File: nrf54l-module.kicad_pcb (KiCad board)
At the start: 4 copper layers, 16 x 25 mm, 137 parts, among them SW1 TS24CA, U1 NRF54L15-QFAA-R, U2 XL-0201SURC, U4 XL-0201SURC, U5 XL-0201SURC, U6 TLV62569DRLR, X1 XL7EL89CKI-111YLC-32M

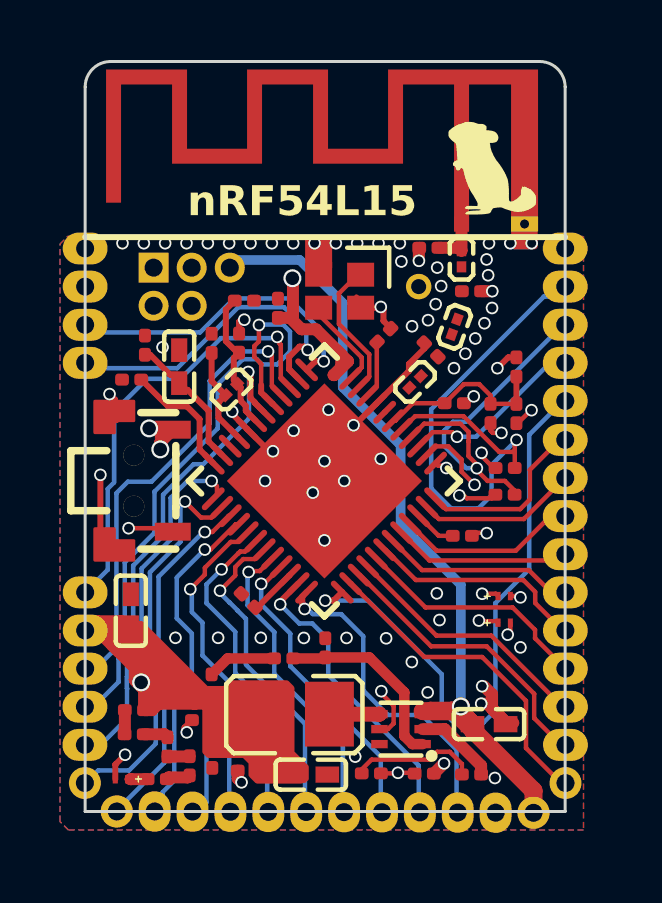
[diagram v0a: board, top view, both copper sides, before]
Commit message: feat: additinal button on P1.12
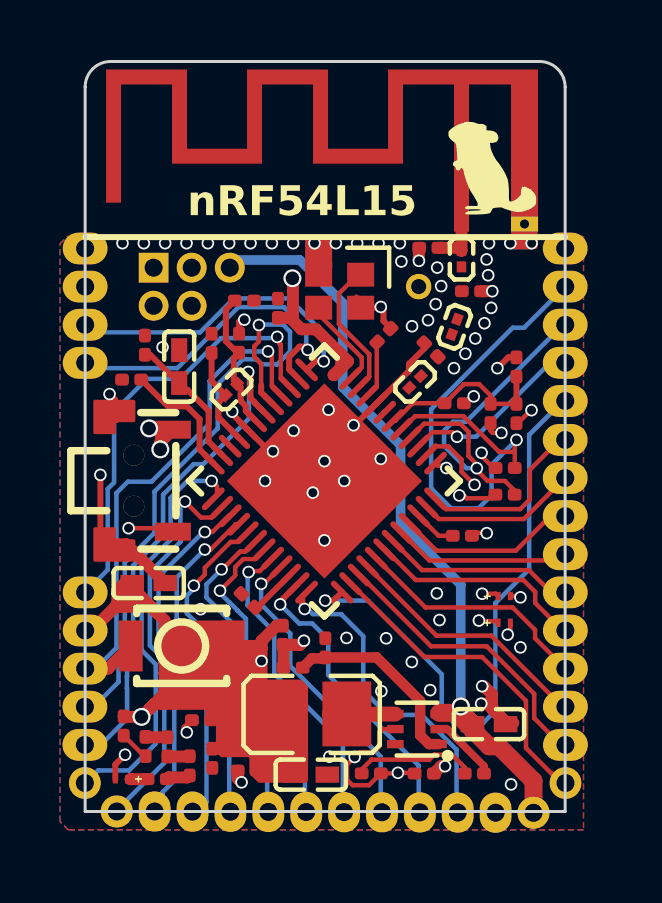
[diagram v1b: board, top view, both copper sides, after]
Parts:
- added SW2: TD-1183SN-1.7H-250, easyeda2kicad:KEY-SMD_B3U-1000PM, F.Cu at (29.0, 39.7)
- moved R3 2.87 mm to (32.4, 39.4), turned to -90 degrees
- moved C18 1.10 mm to (27.9, 37.6), turned to 0 degrees
- moved R14 0.64 mm to (27.1, 42.4), turned to 90 degrees
- moved L4 0.58 mm to (33.4, 42.0)
- moved R13 0.56 mm to (27.8, 43.1), turned to -90 degrees
- moved U6 0.53 mm to (36.9, 42.5)
- moved R4 0.44 mm to (32.7, 40.5)
- moved kibuzzard-68448BA2 0.18 mm to (27.8, 30.3)
- moved R10 0.10 mm to (38.8, 44.0)
- moved kibuzzard-684616DE 0.05 mm to (30.8, 29.4)
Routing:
- net +1V8: track 66.6 -> 90.6 mm, vias 4 -> 5
- net VIN: track 33.7 -> 29.7 mm
- net SW_EN: track 24.2 -> 26.8 mm, vias 2 -> 3
- net P1.12: track 16.4 -> 18.2 mm
- net GND: track 34.2 -> 35.9 mm, vias 70 -> 67
- net Net-(U6-SW): track 1.67 -> 2.78 mm
- net Net-(R3-Pad2): track 2.30 -> 1.53 mm, vias 0 -> 1

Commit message: chore: refactoring
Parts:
- moved U2 0.42 mm to (27.1, 43.8), turned to -90 degrees
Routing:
- net GND: track 35.9 -> 35.3 mm

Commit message: feat: 6 layer because it's cheaper lol wtf
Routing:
- added copper zone on In3.Cu, net GND
- added copper zone on In4.Cu, net GND
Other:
- copper layers 4 -> 6

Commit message: chore: refactoring
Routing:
- net GND: track 35.3 -> 39.9 mm

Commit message: chore: checkpoint
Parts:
- removed the ? at (28.1, 28.4)
- removed the ? at (36.9, 27.8)
- removed the ? at (29.4, 28.4)
- removed the ? at (29.4, 27.1)
- removed the ? at (28.1, 27.1)
- removed the ? at (30.6, 27.1)
- removed C13: 1.5pF, Capacitor_SMD:C_0201_0603Metric
- removed kibuzzard-68448B88: G***, kibuzzard-68448B88
- removed kibuzzard-68449000: G***, kibuzzard-68449000
- removed kibuzzard-6846144B: G***, kibuzzard-6846144B
- removed kibuzzard-68461451: G***, kibuzzard-68461451
- removed kibuzzard-68461457: G***, kibuzzard-68461457
- removed kibuzzard-684616DE: G***, kibuzzard-684616DE
- removed kibuzzard-6846173A: G***, kibuzzard-6846173A
- removed kibuzzard-68461772: G***, kibuzzard-68461772
- removed kibuzzard-68461788: G***, kibuzzard-68461788
- removed kibuzzard-68463A73: G***, kibuzzard-68463A73
- removed kibuzzard-68463A78: G***, kibuzzard-68463A78
- removed kibuzzard-68463A7B: G***, kibuzzard-68463A7B
- removed kibuzzard-68463A81: G***, kibuzzard-68463A81
- removed kibuzzard-68463A85: G***, kibuzzard-68463A85
- added ?: , , F.Cu at (25.8, 36.6)
- added ?: , , F.Cu at (25.8, 32.8)
- added ?: , , F.Cu at (25.8, 35.4)
- added ?: , , F.Cu at (25.8, 31.6)
- added ?: , , F.Cu at (25.8, 34.1)
- added C23: 10uF, easyeda2kicad:C0402, F.Cu at (30.1, 39.3)
- added J1: BM28B0.6-10DS/2-0.35V(51), easyeda2kicad:CONN-SMD_BM28B0.6-10DS-2-0.35V-51, F.Cu at (29.4, 27.8)
- added R15: 1kΩ, Resistor_SMD:R_0201_0603Metric, F.Cu at (39.0, 38.3)
- added R16: 1kΩ, Resistor_SMD:R_0201_0603Metric, F.Cu at (39.0, 39.7)
- added U3: XL-0201SURC, easyeda2kicad:LED-SMD_L0.65-W0.35-P0.41_XL-0201SURC, F.Cu at (38.3, 37.7)
- added U7: XL-0201SURC, easyeda2kicad:LED-SMD_L0.65-W0.35-P0.41_XL-0201SURC, F.Cu at (38.3, 39.1)
- added kibuzzard-68478C96: G***, kibuzzard-68478C96, B.Cu at (27.8, 29.1)
- added kibuzzard-68478D5A: G***, kibuzzard-68478D5A, B.Cu at (27.3, 26.5)
- added kibuzzard-68478D5E: G***, kibuzzard-68478D5E, B.Cu at (28.4, 27.8)
- added kibuzzard-68478D64: G***, kibuzzard-68478D64, B.Cu at (27.8, 31.6)
- added kibuzzard-68478D6B: G***, kibuzzard-68478D6B, B.Cu at (27.8, 32.8)
- added kibuzzard-68478D71: G***, kibuzzard-68478D71, B.Cu at (27.2, 34.1)
- added kibuzzard-68478D74: G***, kibuzzard-68478D74, B.Cu at (27.2, 35.4)
- added kibuzzard-68478D78: G***, kibuzzard-68478D78, B.Cu at (27.8, 36.6)
- added kibuzzard-68478D82: G***, kibuzzard-68478D82, B.Cu at (27.8, 38.0)
- added kibuzzard-68478D86: G***, kibuzzard-68478D86, B.Cu at (27.3, 39.2)
- added kibuzzard-68478D8D: G***, kibuzzard-68478D8D, B.Cu at (27.8, 40.5)
- added kibuzzard-68478D98: G***, kibuzzard-68478D98, B.Cu at (27.8, 41.8)
- added kibuzzard-68478D9B: G***, kibuzzard-68478D9B, B.Cu at (27.8, 43.1)
- L2, L3: value LQP03TN3N5B02D -> MLG0603P2N7CT000
- SW1: value TS24CA -> ~; footprint easyeda2kicad:SW-SMD_TS24CA -> easyeda2kicad:KEY-SMD_B3U-1000PM
- SW2: value TD-1183SN-1.7H-250 -> ~
- moved G*** 11.2 mm to (28.8, 23.1)
- moved kibuzzard-6844924F 4.73 mm to (33.9, 33.9)
- moved kibuzzard-68449253 4.73 mm to (36.3, 34.5)
- moved kibuzzard-684623CD 4.73 mm to (35.1, 34.5)
- moved kibuzzard-68449359 4.32 mm to (32.1, 38.5)
- moved kibuzzard-68449351 4.32 mm to (34.5, 38.5)
- moved kibuzzard-68449360 4.32 mm to (33.3, 38.5)
- moved C18 3.61 mm to (28.8, 41.2), turned to 180 degrees
- moved C7 2.36 mm to (39.4, 27.5), turned to 0 degrees
- moved SW2 1.94 mm to (27.9, 38.1), turned to 90 degrees
- moved C5 1.86 mm to (30.9, 30.1), turned to -90 degrees
- moved X1 1.25 mm to (35.5, 28.3)
- moved C8 1.11 mm to (37.9, 28.6), turned to 170 degrees
- moved G*** 1.10 mm to (40.4, 23.8)
- moved C11 1.03 mm to (33.3, 28.6)
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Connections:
- AE1 pad 2: (no net) -> GND
- SW1 pad 1: GND -> +1V8
- SW1 pad 2: GND -> nRESET
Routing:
- net P0.04: track 18.9 -> 38.3 mm, vias 1 -> 2
- net P0.02: track 6.39 -> 25.1 mm, vias 1 -> 2
- net P0.03: track 12.8 -> 31.3 mm, vias 1 -> 2
- net +1V8: track 90.6 -> 109.1 mm, vias 5 -> 11
- net SWDCLK: track 15.0 -> 32.8 mm, vias 1 -> 3
- net SWDIO: track 12.5 -> 26.5 mm, vias 1 -> 2
- net VIN: track 29.7 -> 39.6 mm
- net GND: track 39.9 -> 32.0 mm, vias 67 -> 80
- net P1.11: track 14.7 -> 21.3 mm, vias 1 -> 2
- net P1.09: track 10.5 -> 16.0 mm
- net P1.13: track 20.8 -> 16.5 mm
- net nRESET: track 41.1 -> 44.8 mm, vias 2 -> 3
- net SW_EN: track 26.8 -> 23.7 mm
- net P1.12: track 18.2 -> 21.2 mm, vias 1 -> 2
- net P1.10: track 10.9 -> 13.6 mm, vias 1 -> 2
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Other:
- board size 16 x 25 mm -> 16.4 x 25.2 mm
- board text added: "16"
- board text added: "2.5V ≤ VIN ≤ 5.5V"
- board text removed: "01"
- board text removed: "1.8V ≤ VIN ≤ 5.5V"

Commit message: chore: checkpoint
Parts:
- removed the C14 at (38.1, 31.6)
- removed FB1: BLM03PX121SN1D, easyeda2kicad:L0201
- removed R12, R13, R14, R15, R16: 1kΩ, Resistor_SMD:R_0201_0603Metric
- removed the R2 at (28.2, 44.2)
- removed the U2 at (27.2, 43.8)
- removed U3, U4, U5, U7: XL-0201SURC, easyeda2kicad:LED-SMD_L0.65-W0.35-P0.41_XL-0201SURC
- removed kibuzzard-68448BA2: G***, kibuzzard-68448BA2
- removed kibuzzard-68448DE0: G***, kibuzzard-68448DE0
- removed kibuzzard-68448DE9: G***, kibuzzard-68448DE9
- removed kibuzzard-68448E11: G***, kibuzzard-68448E11
- removed kibuzzard-68448E3B: G***, kibuzzard-68448E3B
- removed kibuzzard-68448E4C: G***, kibuzzard-68448E4C
- removed kibuzzard-68448E55: G***, kibuzzard-68448E55
- removed kibuzzard-684495B0: G***, kibuzzard-684495B0
- removed kibuzzard-684495B4: G***, kibuzzard-684495B4
- removed kibuzzard-684495B8: G***, kibuzzard-684495B8
- removed kibuzzard-684617E6: G***, kibuzzard-684617E6
- removed kibuzzard-684623E2: G***, kibuzzard-684623E2
- removed kibuzzard-68478C96: G***, kibuzzard-68478C96
- removed kibuzzard-68478D64: G***, kibuzzard-68478D64
- removed kibuzzard-68478D6B: G***, kibuzzard-68478D6B
- removed kibuzzard-68478D74: G***, kibuzzard-68478D74
- removed kibuzzard-68478D78: G***, kibuzzard-68478D78
- removed kibuzzard-68478D82: G***, kibuzzard-68478D82
- added C11: 2.2uF, Capacitor_SMD:C_0201_0603Metric, F.Cu at (30.3, 41.4)
- added LED1: TZ-P2-0402RTIA1-0.45T, easyeda2kicad:LED0402-RD_RED, F.Cu at (27.4, 27.6)
- added LED2: TZ-P2-0402RTIA1-0.45T, easyeda2kicad:LED0402-RD_RED, F.Cu at (28.4, 27.6)
- added LED3: TZ-P2-0402RTIA1-0.45T, easyeda2kicad:LED0402-RD_RED, F.Cu at (27.4, 29.7)
- added LED4: TZ-P2-0402RTIA1-0.45T, easyeda2kicad:LED0402-RD_RED, F.Cu at (28.4, 29.7)
- added R10: 1kΩ, Resistor_SMD:R_0201_0603Metric, F.Cu at (29.7, 28.5)
- added kibuzzard-684F74F9: G***, kibuzzard-684F74F9, B.Cu at (27.8, 29.1)
- added kibuzzard-684F750C: G***, kibuzzard-684F750C, B.Cu at (27.8, 30.3)
- added kibuzzard-684F751D: G***, kibuzzard-684F751D, B.Cu at (27.8, 31.6)
- added kibuzzard-684F753F: G***, kibuzzard-684F753F, B.Cu at (27.8, 32.8)
- added kibuzzard-684F7560: G***, kibuzzard-684F7560, B.Cu at (27.8, 35.4)
- added kibuzzard-684F7579: G***, kibuzzard-684F7579, B.Cu at (27.8, 36.6)
- added kibuzzard-684F7581: G***, kibuzzard-684F7581, B.Cu at (27.8, 38.0)
- added kibuzzard-684F75DA: G***, kibuzzard-684F75DA, B.Cu at (40.3, 44.3)
- added kibuzzard-684F75DE: G***, kibuzzard-684F75DE, B.Cu at (40.2, 43.0)
- added kibuzzard-684F75E1: G***, kibuzzard-684F75E1, B.Cu at (40.2, 41.8)
- added kibuzzard-684F75E4: G***, kibuzzard-684F75E4, B.Cu at (40.2, 40.5)
- added kibuzzard-684F75E9: G***, kibuzzard-684F75E9, B.Cu at (40.2, 39.2)
- added kibuzzard-684F75ED: G***, kibuzzard-684F75ED, B.Cu at (40.2, 38.0)
- added kibuzzard-684F75F1: G***, kibuzzard-684F75F1, B.Cu at (40.2, 36.7)
- added kibuzzard-684F75F7: G***, kibuzzard-684F75F7, B.Cu at (40.2, 35.4)
- added kibuzzard-684F75FF: G***, kibuzzard-684F75FF, B.Cu at (40.2, 34.1)
- added kibuzzard-684F7617: G***, kibuzzard-684F7617, B.Cu at (40.2, 32.9)
- added kibuzzard-684F761F: G***, kibuzzard-684F761F, B.Cu at (40.3, 31.6)
- moved J1 17.6 mm to (39.6, 42.1), turned to -90 degrees
- moved C14 16.4 mm to (34.4, 27.7), turned to 90 degrees
- moved R11 14.4 mm to (29.7, 29.3), turned to 0 degrees
- moved R7 12.8 mm to (29.7, 27.0)
- moved R9 11.9 mm to (29.7, 27.7)
- moved R8 7.24 mm to (39.2, 39.2), turned to 0 degrees
- moved C20 6.62 mm to (39.2, 38.4), turned to 0 degrees
- moved R5 5.46 mm to (37.3, 44.0), turned to 0 degrees
- moved R6 4.92 mm to (36.5, 39.6), turned to 180 degrees
- moved R4 3.72 mm to (36.5, 40.5), turned to 0 degrees
- moved C7 2.85 mm to (28.3, 44.0)
- moved C13 2.82 mm to (29.9, 33.0), turned to 90 degrees
- moved C5 2.80 mm to (28.1, 41.3), turned to 180 degrees
- moved C9 2.73 mm to (30.0, 31.9)
- moved R2 2.54 mm to (36.1, 41.6), turned to -90 degrees
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- renumbered C12 to C1, C19 to C10, C20 to C12, C10 to C13, C22 to C14, C11 to C15, C2 to C16, C6 to C17, C8 to C18, C7 to C19, C1 to C2, C15 to C20, C16 to C21, C9 to C22, C5 to C3, C17 to C4, C23 to C5, C4 to C6, C18 to C7, C21 to C8, C3 to C9, L4 to L1, L1 to L2, L2 to L3, L3 to L4, R3 to R1, R6 to R2, R4 to R3, R9 to R4, R10 to R6, R8 to R7, R1 to R8, R7 to R9, U6 to U1, U1 to U2
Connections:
- ? pad 1: P0.00 -> P2.10
- ? pad 1: P0.01 -> P0.00
- ? pad 1: P2.10 -> P2.09
- ? pad 1: P2.05 -> P2.04
- ? pad 1: SW_EN -> nRESET
- ? pad 1: SWDIO -> P1.10
- ? pad 1: P2.09 -> P2.08
- ? pad 1: P2.02 -> P0.01
- ? pad 1: P2.03 -> P2.02
- ? pad 1: P2.07 -> P2.06
- ? pad 1: P1.09 -> SWDCLK
- ? pad 1: nRESET -> P1.11
- ? pad 1: P2.06 -> P2.05
- ? pad 1: P2.04 -> P2.03
- ? pad 1: SWDCLK -> SWDIO
- ? pad 1: P1.10 -> P1.09
- ? pad 1: P1.11 -> SW_EN
- ? pad 1: P2.08 -> P2.07
- J1 pad 1: P0.04 -> P2.04
- J1 pad 2: P0.03 -> P2.03
- J1 pad 3: P0.02 -> P1.05
- J1 pad 4: P1.10 -> P1.06
- J1 pad 5: P1.09 -> P1.07
- J1 pad 7: P1.11 -> P2.02
- R11 pad 2: Net-(R11-Pad2) -> P1.01
- R7 pad 2: P0.03 -> P0.00
- R9 pad 2: P0.04 -> P0.01
- SW2 pad 2: P1.12 -> P1.11
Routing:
- net P0.04: track 38.3 -> 7.11 mm, vias 2 -> 0
- net GND_LED: track 34.1 -> 8.27 mm, vias 2 -> 1
- net P0.03: track 31.3 -> 6.06 mm, vias 2 -> 0
- net +1V8: track 109.1 -> 86.3 mm, vias 11 -> 7
- net nRESET: track 44.8 -> 22.1 mm, vias 3 -> 1
- net P0.02: track 25.1 -> 5.37 mm, vias 2 -> 0
- net P1.01: track 14.1 -> 32.8 mm, vias 1 -> 2
- net P0.00: track 5.32 -> 22.9 mm, vias 0 -> 1
- net GND: track 32.0 -> 15.1 mm, vias 80 -> 83
- net P1.00: track 13.9 -> 29.1 mm, vias 1 -> 2
- net P0.01: track 6.50 -> 20.3 mm, vias 0 -> 2
- net P1.06: track 11.2 -> 22.9 mm, vias 1 -> 2
- net P1.05: track 10.9 -> 21.5 mm, vias 1 -> 2
- net P1.07: track 10.9 -> 19.1 mm, vias 1 -> 2
- net P2.02: track 21.4 -> 14.0 mm
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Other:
- board size 16.4 x 25.2 mm -> 16.4 x 25.3 mm
- board text added: "1665"
- board text removed: "16"
- board text removed: "65"
